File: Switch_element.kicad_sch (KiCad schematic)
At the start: 24 parts, among them IC301 TPS259802ONRGER, IC302 TPS259802ONRGER

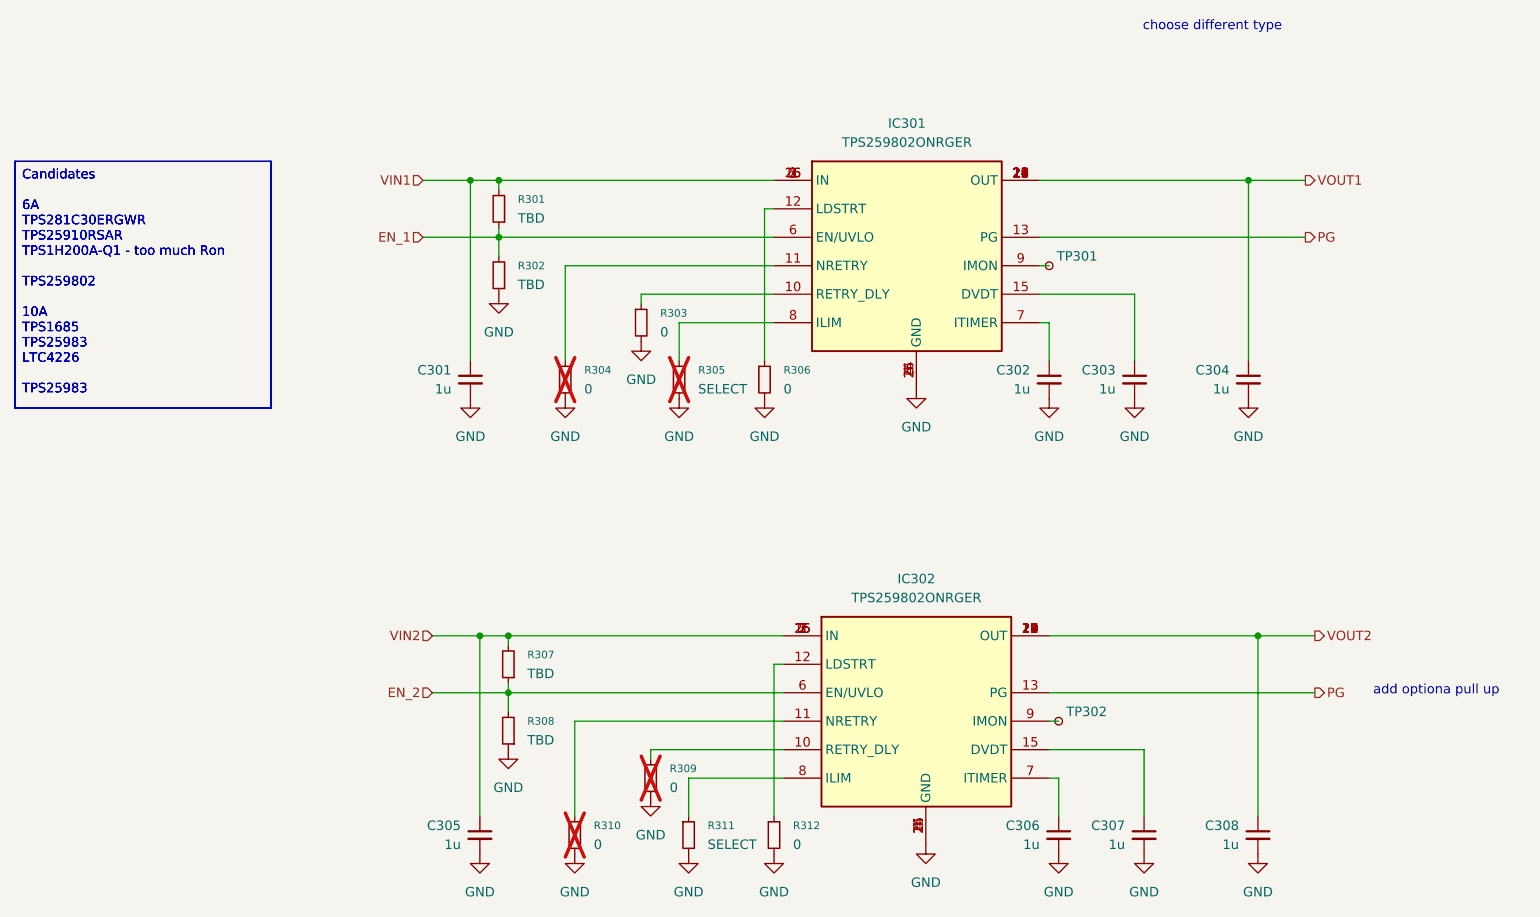
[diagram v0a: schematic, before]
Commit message: pcb progres for all components
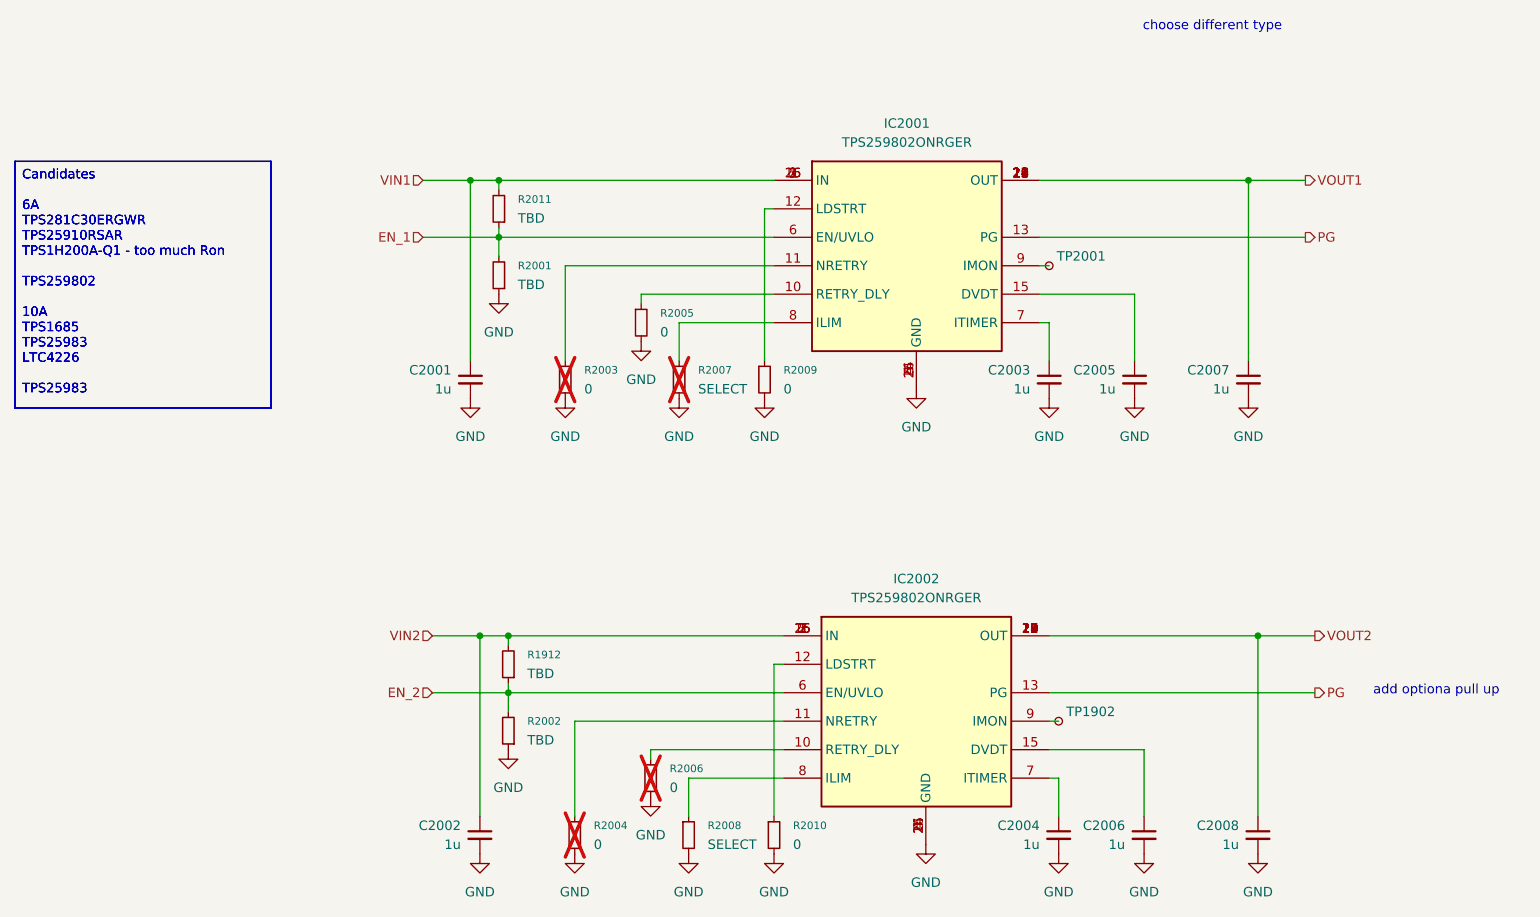
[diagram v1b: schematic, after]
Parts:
- renumbered C301 to C2001, C305 to C2002, C302 to C2003, C306 to C2004, C303 to C2005, C307 to C2006, C304 to C2007, C308 to C2008, IC301 to IC2001, IC302 to IC2002, R307 to R1912, R302 to R2001, R308 to R2002, R304 to R2003, R310 to R2004, R303 to R2005, R309 to R2006, R305 to R2007, R311 to R2008, R306 to R2009, R312 to R2010, R301 to R2011, TP302 to TP1902, TP301 to TP2001

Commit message: progress on PCBs
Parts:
- renumbered C2001 to C801, C2003 to C802, C2005 to C803, C2007 to C804, C2002 to C805, C2004 to C806, C2006 to C807, C2008 to C808, IC2001 to IC801, IC2002 to IC802, R2011 to R801, R2001 to R802, R2005 to R803, R2003 to R804, R2007 to R805, R2009 to R806, R1912 to R807, R2002 to R808, R2006 to R809, R2004 to R810, R2008 to R811, R2010 to R812, TP2001 to TP801, TP1902 to TP802
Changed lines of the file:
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@@
 		(on_board yes)
 		(dnp no)
-		(property "Reference" "C?"
+		(property "Reference" "C802"
 			(at 180.34 67.3162 0)
 			(effects
@@
 		(on_board yes)
 		(dnp no)
-		(property "Reference" "TP?"
+		(property "Reference" "TP801"
 			(at 183.896 52.0699 0)
 			(effects
@@
 		(dnp no)
 		(fields_autoplaced yes)
-		(property "Reference" "#PWR?"
+		(property "Reference" "#PWR0803"
 			(at 165.1 76.2 0)
 			(effects
@@
 		(dnp no)
 		(fields_autoplaced yes)
-		(property "Reference" "#PWR?"
+		(property "Reference" "#PWR0811"
 			(at 110.49 124.46 0)
 			(effects
@@
 		(on_board yes)
 		(dnp no)
-		(property "Reference" "C?"
+		(property "Reference" "C801"
 			(at 102.87 67.3162 0)
 			(effects
@@
 		(dnp no)
 		(fields_autoplaced yes)
-		(property "Reference" "#PWR?"
+		(property "Reference" "#PWR0810"
 			(at 209.55 77.47 0)
 			(effects
@@
 		(dnp no)
 		(fields_autoplaced yes)
-		(property "Reference" "R?"
+		(property "Reference" "R802"
 			(at 111.76 53.3399 0)
 			(effects
@@
 		(dnp no)
 		(fields_autoplaced yes)
-		(property "Reference" "#PWR?"
+		(property "Reference" "#PWR0804"
 			(at 105.41 77.47 0)
 			(effects
@@
 		(dnp no)
 		(fields_autoplaced yes)
-		(property "Reference" "IC?"
+		(property "Reference" "IC802"
 			(at 165.1 95.25 0)
 			(effects
@@
 		(dnp no)
 		(fields_autoplaced yes)
-		(property "Reference" "#PWR?"
+		(property "Reference" "#PWR0807"
 			(at 144.78 77.47 0)
 			(effects
@@
 		(dnp yes)
 		(fields_autoplaced yes)
-		(property "Reference" "R?"
+		(property "Reference" "R810"
 			(at 121.92 128.2699 0)
 			(effects
@@
 		(on_board yes)
 		(dnp no)
-		(property "Reference" "C?"
+		(property "Reference" "C803"
 			(at 191.77 67.3162 0)
 			(effects
@@
 		(dnp no)
 		(fields_autoplaced yes)
-		(property "Reference" "#PWR?"
+		(property "Reference" "#PWR0809"
 			(at 194.31 77.47 0)
 			(effects
@@
 		(dnp no)
 		(fields_autoplaced yes)
-		(property "Reference" "#PWR?"
+		(property "Reference" "#PWR0801"
 			(at 109.22 63.5 0)
 			(effects
@@
 		(on_board yes)
 		(dnp no)
-		(property "Reference" "C?"
+		(property "Reference" "C804"
 			(at 207.01 67.3162 0)
 			(effects
@@
 		(dnp no)
 		(fields_autoplaced yes)
-		(property "Reference" "R?"
+		(property "Reference" "R806"
 			(at 147.32 67.3099 0)
 			(effects
@@
 		(on_board yes)
 		(dnp no)
-		(property "Reference" "TP?"
+		(property "Reference" "TP802"
 			(at 185.166 113.0299 0)
 			(effects
@@
 		(dnp no)
 		(fields_autoplaced yes)
-		(property "Reference" "R?"
+		(property "Reference" "R811"
 			(at 137.16 128.2699 0)
 			(effects
@@
 		(on_board yes)
 		(dnp no)
-		(property "Reference" "C?"
+		(property "Reference" "C806"
 			(at 181.61 128.2762 0)
 			(effects
@@
 		(on_board yes)
 		(dnp no)
-		(property "Reference" "C?"
+		(property "Reference" "C808"
 			(at 208.28 128.2762 0)
 			(effects
@@
 		(dnp yes)
 		(fields_autoplaced yes)
-		(property "Reference" "R?"
+		(property "Reference" "R804"
 			(at 120.65 67.3099 0)
 			(effects
@@
 		(dnp no)
 		(fields_autoplaced yes)
-		(property "Reference" "#PWR?"
+		(property "Reference" "#PWR0813"
 			(at 166.37 137.16 0)
 			(effects
@@
 		(dnp no)
 		(fields_autoplaced yes)
-		(property "Reference" "#PWR?"
+		(property "Reference" "#PWR0819"
 			(at 195.58 138.43 0)
 			(effects
@@
 		(dnp no)
 		(fields_autoplaced yes)
-		(property "Reference" "#PWR?"
+		(property "Reference" "#PWR0812"
 			(at 129.54 130.81 0)
 			(effects
@@
 		(dnp no)
 		(fields_autoplaced yes)
-		(property "Reference" "R?"
+		(property "Reference" "R808"
 			(at 113.03 114.2999 0)
 			(effects
@@
 		(dnp no)
 		(fields_autoplaced yes)
-		(property "Reference" "#PWR?"
+		(property "Reference" "#PWR0816"
 			(at 134.62 138.43 0)
 			(effects
@@
 		(on_board yes)
 		(dnp no)
-		(property "Reference" "C?"
+		(property "Reference" "C805"
 			(at 104.14 128.2762 0)
 			(effects
@@
 		(dnp yes)
 		(fields_autoplaced yes)
-		(property "Reference" "R?"
+		(property "Reference" "R805"
 			(at 135.89 67.3099 0)
 			(effects
@@
 		(dnp no)
 		(fields_autoplaced yes)
-		(property "Reference" "#PWR?"
+		(property "Reference" "#PWR0814"
 			(at 106.68 138.43 0)
 			(effects
@@
 		(dnp no)
 		(fields_autoplaced yes)
-		(property "Reference" "R?"
+		(property "Reference" "R803"
 			(at 130.81 59.6899 0)
 			(effects
@@
 		(dnp no)
 		(fields_autoplaced yes)
-		(property "Reference" "#PWR?"
+		(property "Reference" "#PWR0818"
 			(at 184.15 138.43 0)
 			(effects
@@
 		(dnp no)
 		(fields_autoplaced yes)
-		(property "Reference" "#PWR?"
+		(property "Reference" "#PWR0802"
 			(at 128.27 69.85 0)
 			(effects
@@
 		(dnp no)
 		(fields_autoplaced yes)
-		(property "Reference" "#PWR?"
+		(property "Reference" "#PWR0820"
 			(at 210.82 138.43 0)
 			(effects
@@
 		(dnp no)
 		(fields_autoplaced yes)
-		(property "Reference" "IC?"
+		(property "Reference" "IC801"
 			(at 163.83 34.29 0)
 			(effects
@@
 		(dnp no)
 		(fields_autoplaced yes)
-		(property "Reference" "#PWR?"
+		(property "Reference" "#PWR0815"
 			(at 119.38 138.43 0)
 			(effects
@@
 		(dnp no)
 		(fields_autoplaced yes)
-		(property "Reference" "#PWR?"
+		(property "Reference" "#PWR0806"
 			(at 133.35 77.47 0)
 			(effects
@@
 		(dnp no)
 		(fields_autoplaced yes)
-		(property "Reference" "R?"
+		(property "Reference" "R801"
 			(at 111.76 44.4499 0)
 			(effects
@@
 		(dnp no)
 		(fields_autoplaced yes)
-		(property "Reference" "#PWR?"
+		(property "Reference" "#PWR0817"
 			(at 146.05 138.43 0)
 			(effects
@@
 		(on_board yes)
 		(dnp no)
-		(property "Reference" "C?"
+		(property "Reference" "C807"
 			(at 193.04 128.2762 0)
 			(effects
@@
 		(dnp yes)
 		(fields_autoplaced yes)
-		(property "Reference" "R?"
+		(property "Reference" "R809"
 			(at 132.08 120.6499 0)
 			(effects
@@
 		(dnp no)
 		(fields_autoplaced yes)
-		(property "Reference" "#PWR?"
+		(property "Reference" "#PWR0805"
 			(at 118.11 77.47 0)
 			(effects
@@
 		(dnp no)
 		(fields_autoplaced yes)
-		(property "Reference" "R?"
+		(property "Reference" "R812"
 			(at 148.59 128.2699 0)
 			(effects
@@
 		(dnp no)
 		(fields_autoplaced yes)
-		(property "Reference" "R?"
+		(property "Reference" "R807"
 			(at 113.03 105.4099 0)
 			(effects
@@
 		(dnp no)
 		(fields_autoplaced yes)
-		(property "Reference" "#PWR?"
+		(property "Reference" "#PWR0808"
 			(at 182.88 77.47 0)
 			(effects
